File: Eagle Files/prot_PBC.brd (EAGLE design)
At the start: 36.8 x 64.4 mm, 24 parts

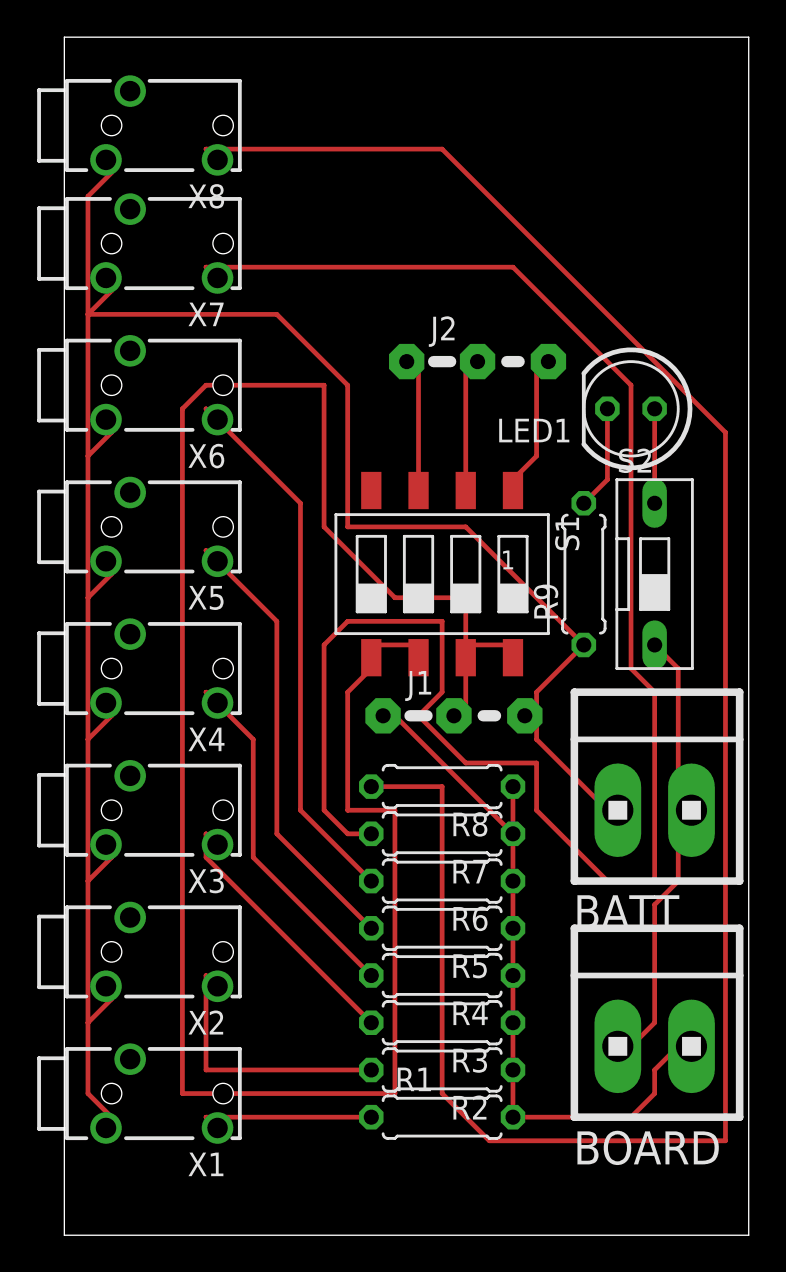
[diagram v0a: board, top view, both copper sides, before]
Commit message: 
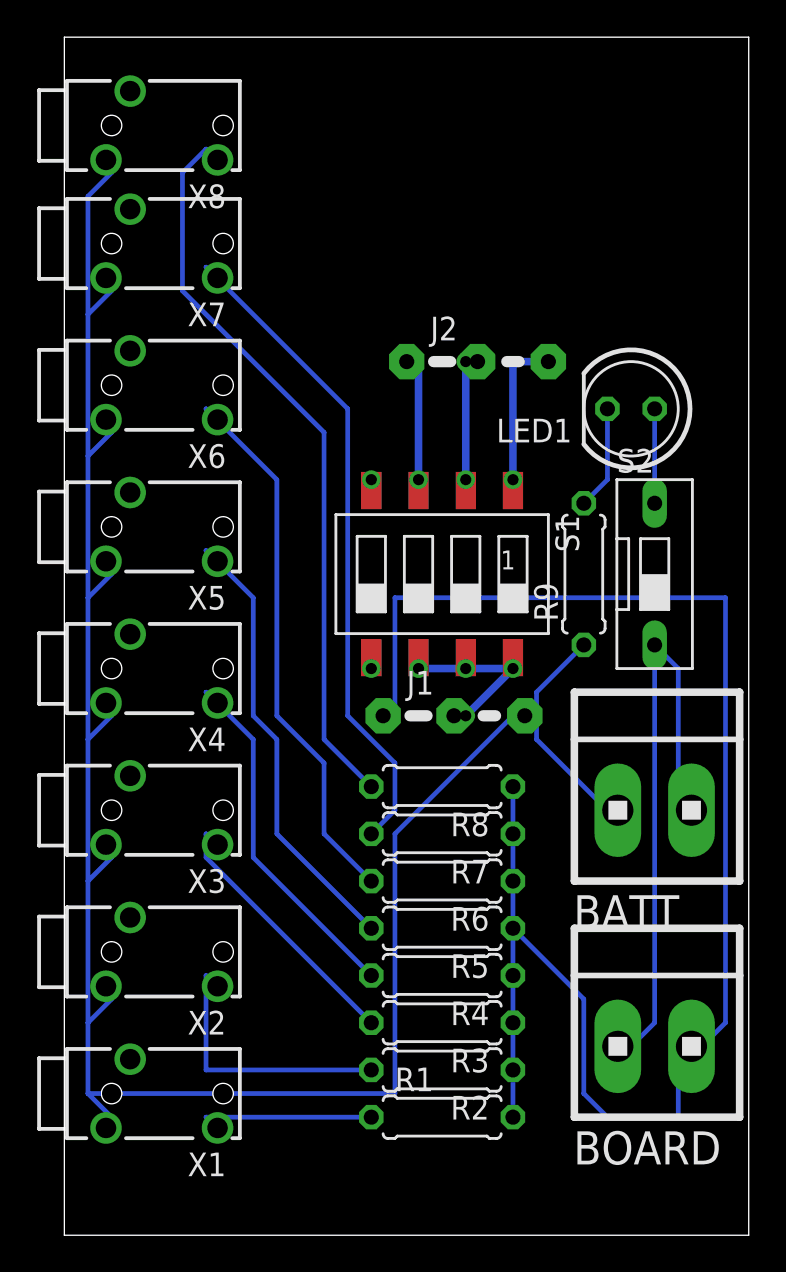
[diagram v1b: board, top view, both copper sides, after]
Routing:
- net VCC/GND: track 113.9 -> 9.31 mm, vias 0 -> 1
- net ADC_8: track 109.8 -> 39.9 mm
- net ADC_7: track 95.8 -> 36.1 mm
- net VCC: track 39.3 -> 88.4 mm
- net VCC1: track 24.6 -> 33.0 mm
- net GND: track 119.8 -> 121.4 mm
- net ADD_0: track 8.10 -> 8.84 mm
- net ADD_2: track 7.57 -> 6.99 mm
- net ADD_1: track 7.57 -> 6.98 mm, vias 0 -> 1

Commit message: 
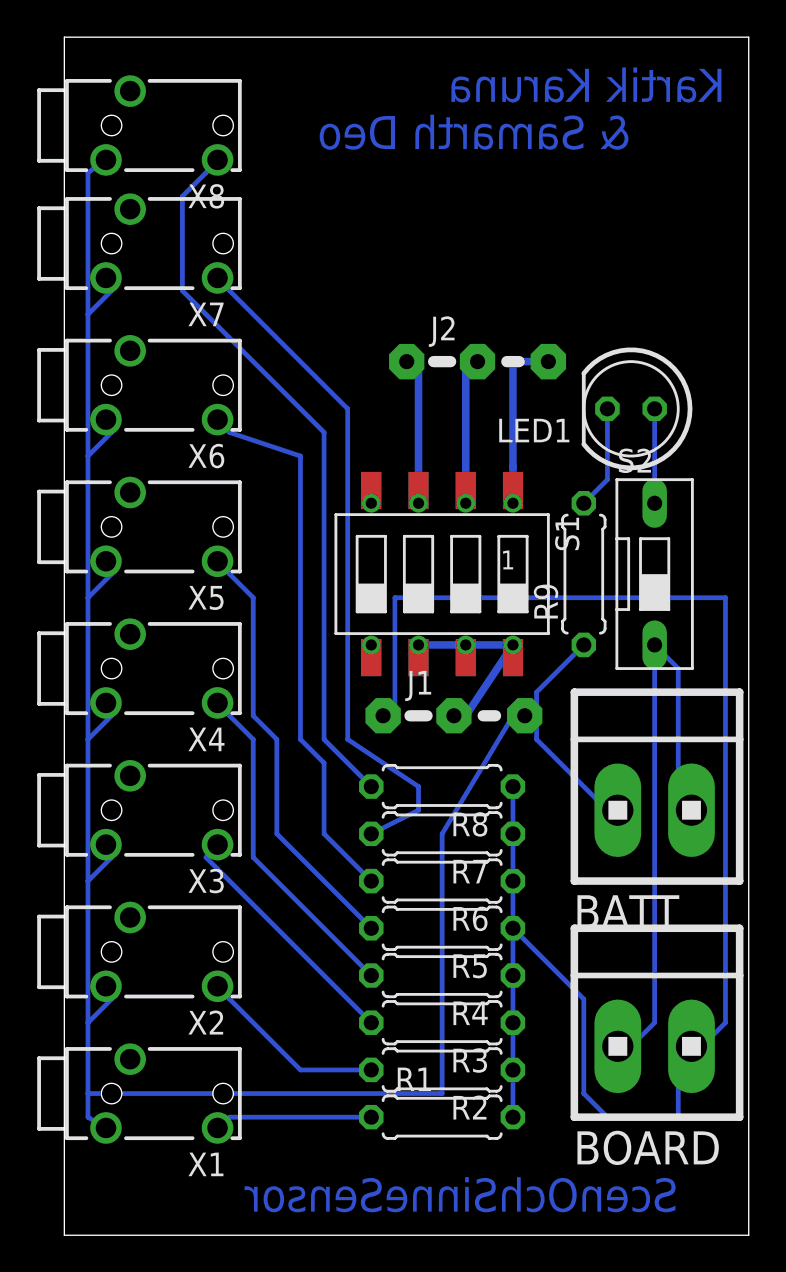
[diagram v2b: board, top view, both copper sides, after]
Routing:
- net ADC_1: track 14.8 -> 10.1 mm
- net ADC_4: track 24.9 -> 23.2 mm
- net ADC_3: track 19.8 -> 18.1 mm
- net ADD_2: track 6.99 -> 8.26 mm, vias 0 -> 1
- net ADD_1: track 6.98 -> 8.26 mm
- net ADC_0: track 9.74 -> 8.49 mm
- net ADC_8: track 39.9 -> 38.7 mm
- net ADC_2: track 14.7 -> 13.5 mm
- net VCC/GND: track 9.31 -> 10.3 mm, vias 1 -> 0
- net GND: track 121.4 -> 122.2 mm
- net ADD_0: track 8.84 -> 9.53 mm, vias 0 -> 1
- net ADC_6: track 29.9 -> 29.4 mm
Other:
- board text added: "& Samarth Deo"
- board text added: "Kartik Karuna"
- board text added: "ScenOchSinneSensor"
